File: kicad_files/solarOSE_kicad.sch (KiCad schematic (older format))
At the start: 9 parts, among them J1 Conn_01x02, J2 Conn_01x02, J3 Conn_01x02, U1 MCP23017_SP, U2 MCP23017_SP, U3 MCP23017_SP, U4 MCP23017_SP

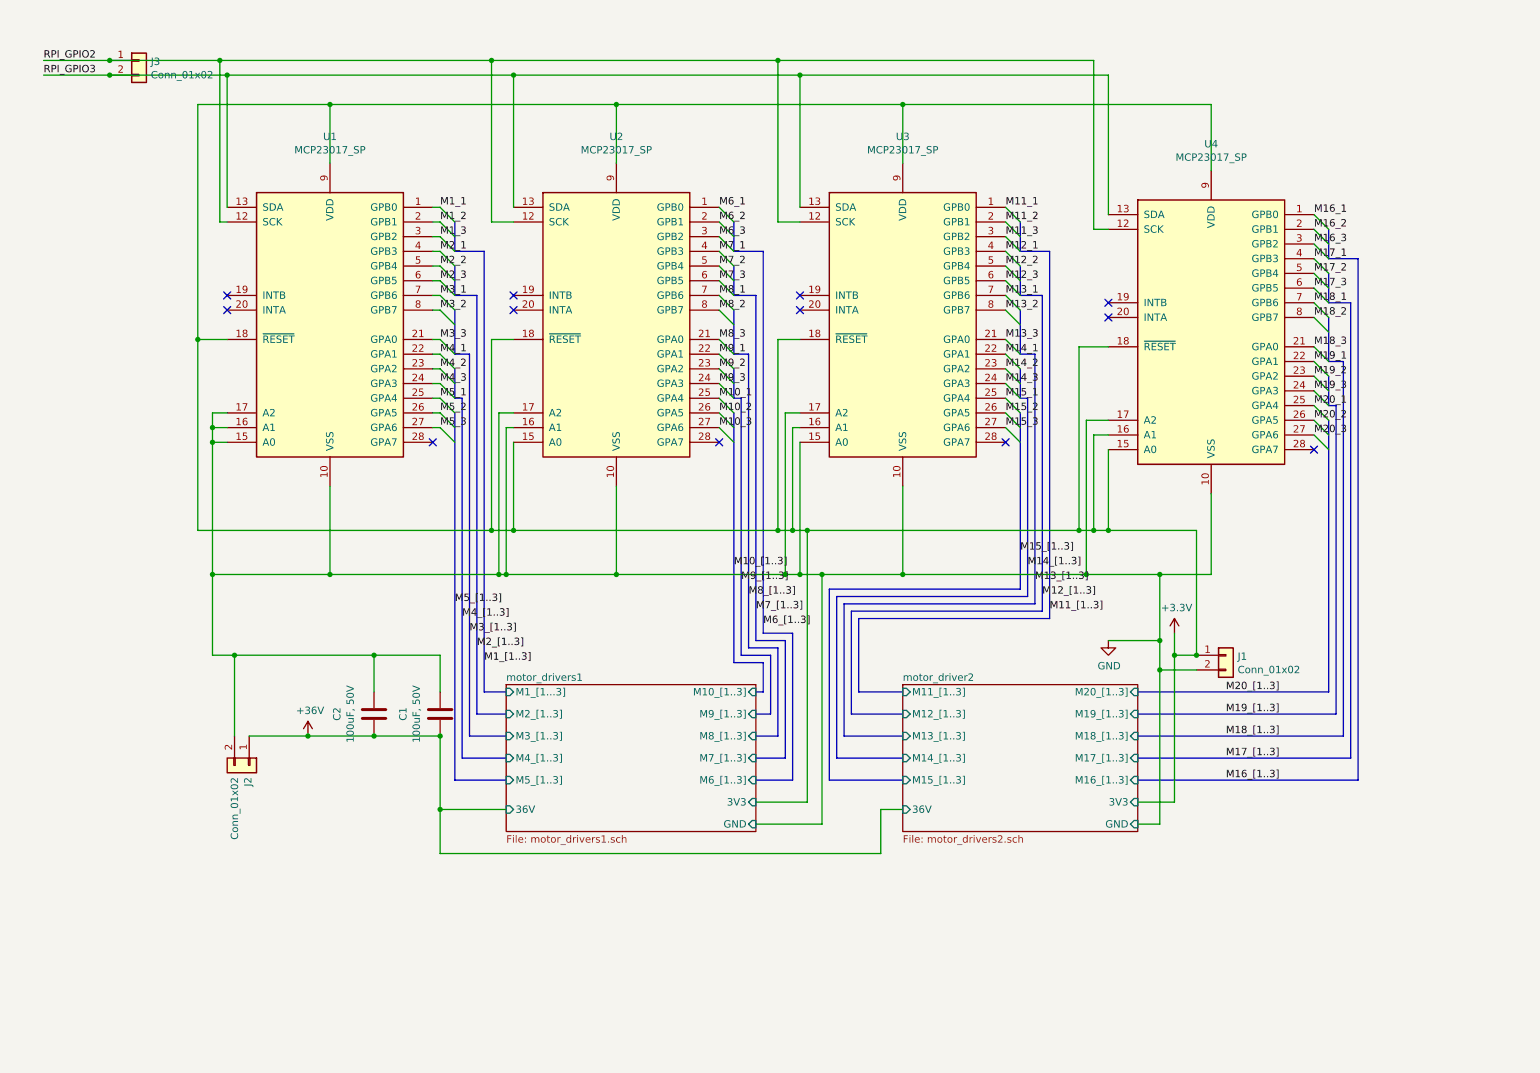
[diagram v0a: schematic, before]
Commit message: version with one card for 5 motors
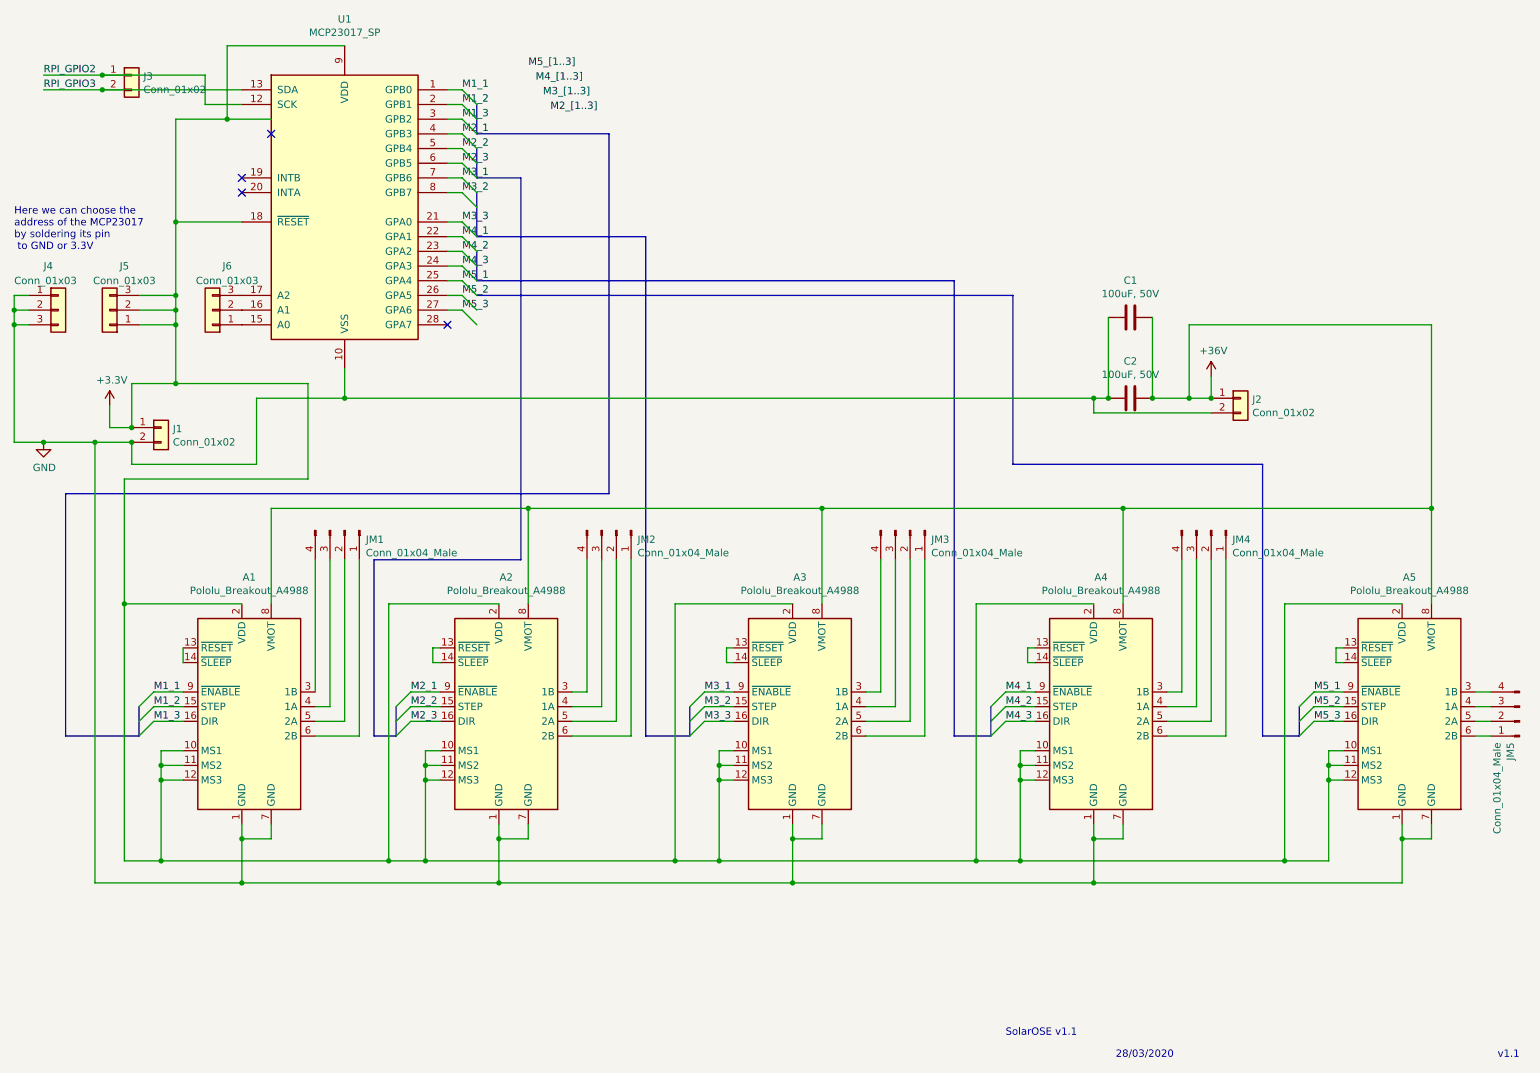
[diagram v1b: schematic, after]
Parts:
- removed U2, U3, U4: MCP23017_SP, Package_DIP:DIP-28_W7.62mm, symbol Interface_Expansion:MCP23017_SP
- added A1, A2, A3, A4, A5: Pololu_Breakout_A4988, Module:Pololu_Breakout-16_15.2x20.3mm, symbol Driver_Motor:Pololu_Breakout_A4988
- added J4, J5, J6: Conn_01x03, Connector_Wire:SolderWirePad_1x03_P3.81mm_Drill1.2mm, symbol Connector_Generic:Conn_01x03
- added JM1, JM2, JM3, JM4, JM5: Conn_01x04_Male, Connector_Wire:SolderWirePad_1x04_P6.35mm_Drill2mm, symbol Connector:Conn_01x04_Male
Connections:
- net +36V: now also C1.1, C2.1, A1.8 (VMOT), A2.8 (VMOT), A3.8 (VMOT), A4.8 (VMOT), A5.8 (VMOT); no longer C1.2, C2.2
- net +3V3: now also U1.11 (NC), A1.10 (MS1), A1.11 (MS2), A1.12 (MS3), A1.2 (VDD), A2.10 (MS1), A2.11 (MS2), A2.12 (MS3), A2.2 (VDD), A3.10 (MS1), A3.11 (MS2), A3.12 (MS3), A3.2 (VDD), A4.10 (MS1), A4.11 (MS2), A4.12 (MS3), A4.2 (VDD), A5.10 (MS1), A5.11 (MS2), A5.12 (MS3), A5.2 (VDD), J5.1 (Pin_1), J5.2 (Pin_2), J5.3 (Pin_3)
- net GND: now also C1.2, C2.2, A1.1 (GND), A1.7 (GND), A2.1 (GND), A2.7 (GND), A3.1 (GND), A3.7 (GND), A4.1 (GND), A4.7 (GND), A5.1 (GND), A5.7 (GND), J4.1 (Pin_1), J4.2 (Pin_2), J4.3 (Pin_3); no longer C1.1, C2.1, U1.15 (A0), U1.16 (A1), U1.17 (A2)
- net M1_1: now also A1.9 (~ENABLE)
- net M1_2: now also A1.15 (STEP)
- net M1_3: now also A1.16 (DIR)
- net M2_1: now also A2.9 (~ENABLE)
- net M2_2: now also A2.15 (STEP)
- net M2_3: now also A2.16 (DIR)
- net M3_1: now also A3.9 (~ENABLE)
- net M3_2: now also A3.15 (STEP)
- net M3_3: now also A3.16 (DIR)
- net M4_1: now also A4.9 (~ENABLE)
- net M4_2: now also A4.15 (STEP)
- net M4_3: now also A4.16 (DIR)
- net M5_1: now also A5.9 (~ENABLE)
- net M5_2: now also A5.15 (STEP)
- net M5_3: now also A5.16 (DIR)
- new net: J6.1 (Pin_1), U1.15 (A0)
- new net: J6.2 (Pin_2), U1.16 (A1)
- new net: J6.3 (Pin_3), U1.17 (A2)
- new net: A1.13 (~RESET), A1.14 (~SLEEP)
- new net: A1.3 (1B), JM1.4 (Pin_4)
- new net: A1.4 (1A), JM1.3 (Pin_3)
- new net: A1.5 (2A), JM1.2 (Pin_2)
- new net: A1.6 (2B), JM1.1 (Pin_1)
- new net: A2.13 (~RESET), A2.14 (~SLEEP)
- new net: A2.3 (1B), JM2.4 (Pin_4)
- new net: A2.4 (1A), JM2.3 (Pin_3)
- new net: A2.5 (2A), JM2.2 (Pin_2)
- new net: A2.6 (2B), JM2.1 (Pin_1)
- new net: A3.13 (~RESET), A3.14 (~SLEEP)
- new net: A3.3 (1B), JM3.4 (Pin_4)
- new net: A3.4 (1A), JM3.3 (Pin_3)
- new net: A3.5 (2A), JM3.2 (Pin_2)
- new net: A3.6 (2B), JM3.1 (Pin_1)
- new net: A4.13 (~RESET), A4.14 (~SLEEP)
- new net: A4.3 (1B), JM4.4 (Pin_4)
- new net: A4.4 (1A), JM4.3 (Pin_3)
- new net: A4.5 (2A), JM4.2 (Pin_2)
- new net: A4.6 (2B), JM4.1 (Pin_1)
- new net: A5.13 (~RESET), A5.14 (~SLEEP)
- new net: A5.3 (1B), JM5.4 (Pin_4)
- new net: A5.4 (1A), JM5.3 (Pin_3)
- new net: A5.5 (2A), JM5.2 (Pin_2)
- new net: A5.6 (2B), JM5.1 (Pin_1)
- no-connect marks 12 -> 4
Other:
- note added: "28/03/2020"
- note added: "Here we can choose the \naddress of the MCP23017 \nby soldering its pin\n to GND or 3.3V"
- note added: "SolarOSE v1.1"
- note added: "v1.1"
- moved on the sheet: J1, J3, U1
